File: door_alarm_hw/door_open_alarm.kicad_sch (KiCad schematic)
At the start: 62 parts, among them Q1 CJ2301 S1, Q2 BSS138PW,115, Q3 CJ2301 S1, SW1 TS-1088-AR02016, SW2 TS-1088-AR02016, SW3 SS-12D10L5, SW4 MET-200, U1 ESP32-S3-MINI-1, U2 AP2114HA-3.3TRG1

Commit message: Overhauling...
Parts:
- removed C1, C6, C7, C8: 1u, pepy_sym_lib:[CAP_SMD]0805_2012Metric, symbol pepy_sym_lib:[CAP_SMD]0805_2012Metric
- removed C2: 10u, pepy_sym_lib:[CAP_SMD]0805_2012Metric, symbol pepy_sym_lib:[CAP_SMD]0805_2012Metric
- removed C3: 0.1u, pepy_sym_lib:[CAP_SMD]0805_2012Metric, symbol pepy_sym_lib:[CAP_SMD]0805_2012Metric
- removed C4, C5: 22u, pepy_sym_lib:[CAP_SMD]0805_2012Metric, symbol pepy_sym_lib:[CAP_SMD]0805_2012Metric
- removed H2, H3, H4: MountingHole_Pad, symbol Mechanical:MountingHole_Pad
- removed R1, R3: 470R, pepy_sym_lib:[RES_SMD]0805_2012Metric, symbol pepy_sym_lib:[RES_SMD]0805_2012Metric
- removed R10: 1k, pepy_sym_lib:[RES_SMD]0805_2012Metric, symbol pepy_sym_lib:[RES_SMD]0805_2012Metric
- removed R11, R9: 15k 1%, pepy_sym_lib:[RES_SMD]0805_2012Metric, symbol pepy_sym_lib:[RES_SMD]0805_2012Metric
- removed R12, R13, R14, R16, R17, R6, R7: 10k, pepy_sym_lib:[RES_SMD]0805_2012Metric, symbol pepy_sym_lib:[RES_SMD]0805_2012Metric
- removed R15: 30k, pepy_sym_lib:[RES_SMD]0805_2012Metric, symbol pepy_sym_lib:[RES_SMD]0805_2012Metric
- removed R2, R4: 5.1k, pepy_sym_lib:[RES_SMD]0805_2012Metric, symbol pepy_sym_lib:[RES_SMD]0805_2012Metric
- removed R5: 1M, pepy_sym_lib:[RES_SMD]0805_2012Metric, symbol pepy_sym_lib:[RES_SMD]0805_2012Metric
- removed R8: 100k, pepy_sym_lib:[RES_SMD]0805_2012Metric, symbol pepy_sym_lib:[RES_SMD]0805_2012Metric
- removed REED_G1: GND, symbol Connector:TestPoint
- removed REED_OUT1: REED_OUT, symbol Connector:TestPoint
- removed TP11: REED, pepy_sym_lib:[TEST_POINT]TestPoint_Pad_D1.0mm, symbol Connector:TestPoint
- removed TP2: 3.3V, pepy_sym_lib:[TEST_POINT]TestPoint_Pad_D1.0mm, symbol Connector:TestPoint
- removed TP6: V_INPUT, pepy_sym_lib:[TEST_POINT]TestPoint_Pad_D1.0mm, symbol Connector:TestPoint
- added C1, C3, C7: CL21A106KOQNNNE, pepy_sym_lib:[CAP_SMD_0805_2012Metric], symbol pepy_sym_lib:[CAP_SMD_0805_2012Metric]Samsung Electro-Mechanics CL21A106KOQNNNE
- added C2, C8: CC0805KRX7R9BB104, pepy_sym_lib:[CAP_SMD_0805_2012Metric], symbol pepy_sym_lib:[CAP_SMD_0805_2012Metric]YAGEO CC0805KRX7R9BB104
- added C4, C5, C6: C0805C105M4VACTU, pepy_sym_lib:[CAP_SMD_0805_2012Metric], symbol pepy_sym_lib:[CAP_SMD_0805_2012Metric]KEMET C0805C105M4VACTU
- added F1: 0466.200NRHF, pepy_sym_lib:[FUSE_SMD_1206], symbol pepy_sym_lib:[FUSE_SMD_1206]Littelfuse 0466.200NRHF
- added MH1, MH2: ~, pepy_sym_lib:[MOUNTING_HOLE]MountingHole_2.2mm_M2_DIN965_Pad, symbol pepy_sym_lib:[MOUNTING_HOLE]MountingHole_Pad
- added R1, R10, R12, R15, R2, R5, R7, R9: 0805W8F1002T5E, pepy_sym_lib:[RES_SMD_0805_2012Metric], symbol pepy_sym_lib:[RES_SMD_0805_2012Metric]UNI-ROYAL(Uniroyal Elec) 0805W8F1002T5E
- added R11: 0805W8F1003T5E, pepy_sym_lib:[RES_SMD_0805_2012Metric], symbol pepy_sym_lib:[RES_SMD_0805_2012Metric]UNI-ROYAL(Uniroyal Elec) 0805W8F1003T5E
- added R13, R3, R4: 0805W8F5101T5E, pepy_sym_lib:[RES_SMD_0805_2012Metric], symbol pepy_sym_lib:[RES_SMD_0805_2012Metric]UNI-ROYAL(Uniroyal Elec) 0805W8F5101T5E
- added R14: 0805W8J0203T5E, pepy_sym_lib:[RES_SMD_0805_2012Metric], symbol pepy_sym_lib:[RES_SMD_0805_2012Metric]UNI-ROYAL(Uniroyal Elec) 0805W8J0203T5E
- added R16, R17: 0805W8F4700T5E, pepy_sym_lib:[RES_SMD_0805_2012Metric], symbol pepy_sym_lib:[RES_SMD_0805_2012Metric]UNI-ROYAL(Uniroyal Elec) 0805W8F4700T5E
- added R6: 0805W8F1004T5E, pepy_sym_lib:[RES_SMD_0805_2012Metric], symbol pepy_sym_lib:[RES_SMD_0805_2012Metric]UNI-ROYAL(Uniroyal Elec) 0805W8F1004T5E
- added R8: 0805W8F1001T5E, pepy_sym_lib:[RES_SMD_0805_2012Metric], symbol pepy_sym_lib:[RES_SMD_0805_2012Metric]UNI-ROYAL(Uniroyal Elec) 0805W8F1001T5E
- added TP5: 3.3V, pepy_sym_lib:[TEST_POINT]TestPoint_Pad_D1.0mm, symbol pepy_sym_lib:[TEST_POINT]TestPoint
- added TP6: GND, pepy_sym_lib:[TEST_POINT]TestPoint_Pad_D1.0mm, symbol pepy_sym_lib:[TEST_POINT]TestPoint
- added TP9: REED, pepy_sym_lib:[TEST_POINT]TestPoint_Pad_D1.0mm, symbol pepy_sym_lib:[TEST_POINT]TestPoint
- D1: renamed from D6; Manufacturer (none) -> STMicroelectronics; Package (none) -> SOD-123
- D2: renamed from D4; Manufacturer (none) -> STMicroelectronics; Package (none) -> SOD-123
- D3: renamed from D1; Manufacturer (none) -> Nexperia; Package (none) -> SOT1176-1
- D4: renamed from D5; Manufacturer (none) -> STMicroelectronics; Package (none) -> SOD-123
- D5: renamed from D2; Manufacturer (none) -> Lite-On; Package (none) -> 0603
- D6: renamed from D3; Manufacturer (none) -> Lite-On; Package (none) -> 0603
- FID1, FID2, FID3: value ~ -> Fiducial; footprint (none) -> Fiducial:Fiducial_0.5mm_Mask1mm
- H1: Manufacturer (none) -> XFCN
- J1: renamed from USB1; Manufacturer (none) -> SHOU HAN
- L1: Manufacturer (none) -> Murata Electronics
- Q1: renamed from Q2; Manufacturer (none) -> Nexperia; Package (none) -> SOT-323-3
- Q2: renamed from Q1; Manufacturer (none) -> Jiangsu Changjing Electronics Technology Co., Ltd.; Package (none) -> SOT-23
- Q3: Manufacturer (none) -> Jiangsu Changjing Electronics Technology Co., Ltd.; Package (none) -> SOT-23
- S1: renamed from SW3; Manufacturer (none) -> XKB Connection; Package (none) -> THT
- S2: renamed from SW1; Manufacturer (none) -> XUNPU
- S3: renamed from SW2; Manufacturer (none) -> XUNPU
- SW1: renamed from SW4; value MET-200 -> SW_Reed
- TP11: renamed from TP4; value BOOT0 -> BOOT
- TP2: renamed from TP9; value VCC -> VBAT
- U1: renamed from U2; Manufacturer (none) -> Diodes Incorporated; Package (none) -> SOT-223-3
- U2: renamed from U1; LCSC Part (none) -> C2913206; Manufacturer (none) -> Espressif Systems; Package (none) -> SMD-41P
- renumbered TP8 to TP10, TP10 to TP3, TP5 to TP4, TP3 to TP7, TP7 to TP8
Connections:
- net +3.3V: now also C3.1, C7.1, C8.2, R1.2, R10.2, R12.2, R15.2, TP5.1
- net BOOT0: now also C5.2, R15.1
- net EN: now also R11.1
- net ESP_RESET: now also C4.2, R10.1
- net GND: now also D5.2 (C), D6.2 (C), C1.2, C2.2, C3.2, C4.1, C5.1, C6.1, C7.2, C8.1, MH1.1, MH2.1, R14.1, R2.1, R3.1, R4.1, R5.1, R6.2, R7.1, R9.1, TP6.1; no longer D5.1 (K), D6.1 (K)
- net LED_EN: now also R17.2
- net MEAS_EN: now also R8.1
- net REED: now also TP9.1
- net SHIELD: now also C2.1, R6.1
- net STRAP_3: now also R1.1, R2.2
- net STRAP_45: now also R5.2
- net STRAP_46: now also R7.2
- net VBUS: now also R16.2
- net VCC: now also F1.1; no longer S1.2
- net V_INPUT: now also C1.1, R11.2
- net V_SENSE: now also C6.2, R13.1, R14.2
- net at Q3.2 (S): now also R12.1
- net at Q2.3 (D): now also R13.2
- net at Q1.1 (G): now also R8.2, R9.2
- net at J1.10 (CC2): now also R4.2
- net at J1.4 (CC1): now also R3.2
- new net: F1.2, S1.2
- new net: D6.1 (A), R17.1
- new net: D5.1 (A), R16.1
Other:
- moved on the sheet: D1, D2, D3, D4, D5, D6, FID1, FID2, FID3, H1, J1, Q1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

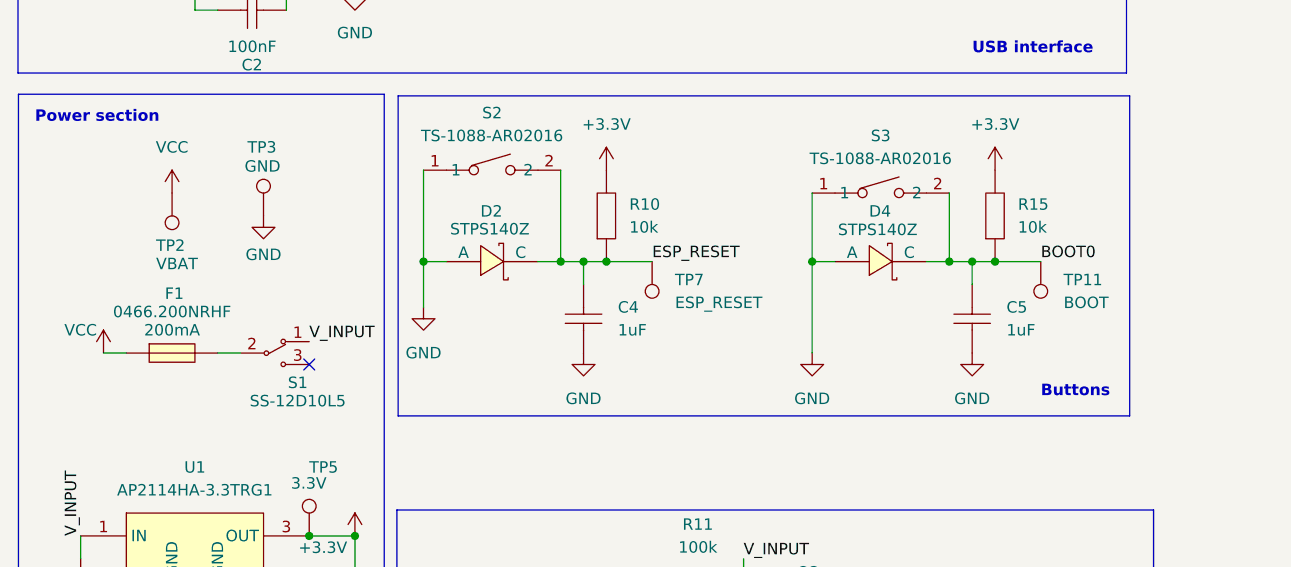
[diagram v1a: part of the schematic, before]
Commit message: Changes due to library update (minor)
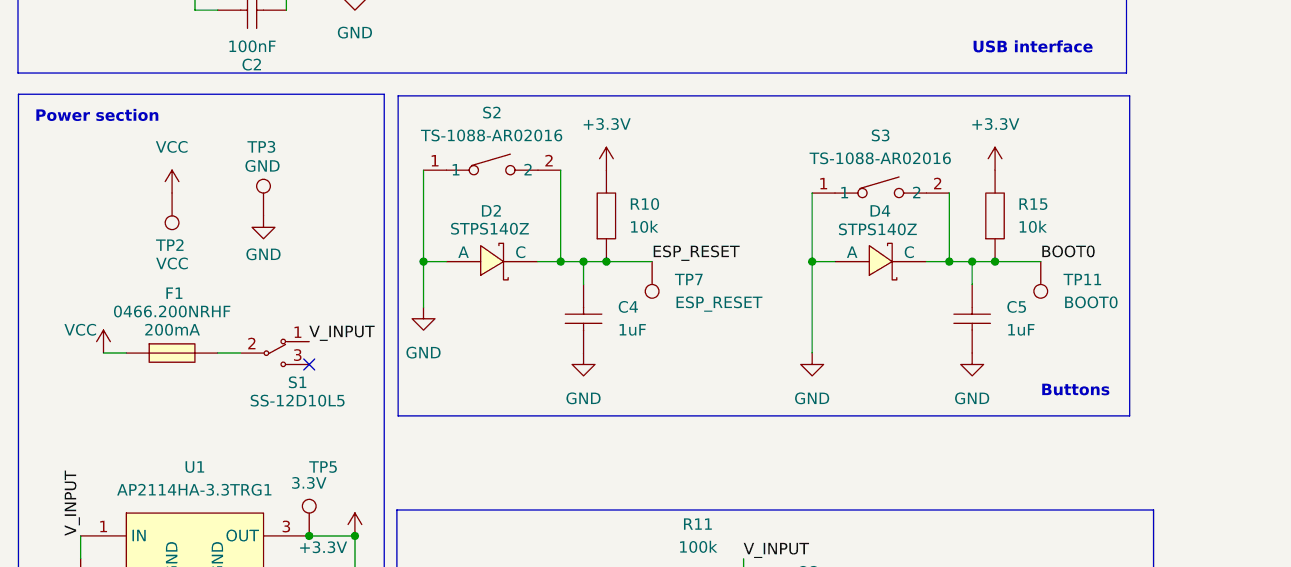
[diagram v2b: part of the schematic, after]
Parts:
- TP11: value BOOT -> BOOT0
- TP2: value VBAT -> VCC
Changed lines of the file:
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@@
 			)
 		)
-		(property "Description" " 20V 2.3A 350mW 112mΩ@4.5V,2.8A 1V@250uA 1PCSPChannel SOT-23 MOSFETs ROHS"
+		(property "Description" "20V 2.3A 350mW 112mΩ@4.5V,2.8A 1V@250uA 1PCSPChannel SOT-23 MOSFETs ROHS"
 			(at 99.06 223.52 0)
 			(effects
@@
 			)
 		)
-		(property "Description" "16V 10uF X5R ±10% 0805 Multilayer Ceramic Capacitors MLCC - SMD/SMT ROHS "
+		(property "Description" "16V 10uF X5R ±10% 0805 Multilayer Ceramic Capacitors MLCC - SMD/SMT ROHS"
 			(at 293.624 107.95 0)
 			(effects
@@
 			)
 		)
-		(property "Description" "16V 10uF X5R ±10% 0805 Multilayer Ceramic Capacitors MLCC - SMD/SMT ROHS "
+		(property "Description" "16V 10uF X5R ±10% 0805 Multilayer Ceramic Capacitors MLCC - SMD/SMT ROHS"
 			(at 39.624 163.83 0)
 			(effects
@@
 		)
 		(property "Description" "Smallsized module supporting 2.4 GHz WiFi (802.11 b/g/n) and Bluetooth ® 5 (LE) Built around ESP32S3 series of SoCs, Xtensa ® dualcore 32bit LX7 microprocessor Flash up to 8 MB, optional 2 MB PSRAM in chip package 39 GPIOs, rich set of peripherals Onboard PCB antenna or external antenna connector"
-			(at 236.22 66.04 0)
+			(at 236.982 119.38 0)
 			(effects
 				(font
@@
 		)
 		(property "LCSC Part" "C2913206"
-			(at 236.22 66.04 0)
+			(at 235.458 128.016 0)
 			(effects
 				(font
@@
 			)
 		)
-		(property "Description" " 20V 2.3A 350mW 112mΩ@4.5V,2.8A 1V@250uA 1PCSPChannel SOT-23 MOSFETs ROHS"
+		(property "Description" "20V 2.3A 350mW 112mΩ@4.5V,2.8A 1V@250uA 1PCSPChannel SOT-23 MOSFETs ROHS"
 			(at 99.06 165.1 0)
 			(effects
@@
 			)
 		)
-		(property "Value" "BOOT"
+		(property "Value" "BOOT0"
 			(at 132.08 129.032 0)
 			(effects
@@
 			)
 		)
-		(property "Description" " 125mW Thick Film Resistors 150V ±100ppm/℃ ±5% 20kΩ 0805 Chip Resistor - Surface Mount ROHS"
+		(property "Description" "125mW Thick Film Resistors 150V ±100ppm/℃ ±5% 20kΩ 0805 Chip Resistor - Surface Mount ROHS"
 			(at 124.206 177.8 0)
 			(effects
@@
 			)
 		)
-		(property "Description" " 20mA 99mcd Colorless transparent lens -30℃~+85℃ 631nm Red 130° 62.5mW 2V 0603 LED Indication - Discrete ROHS"
+		(property "Description" "20mA 99mcd Colorless transparent lens -30℃~+85℃ 631nm Red 130° 62.5mW 2V 0603 LED Indication - Discrete ROHS"
 			(at 147.32 66.04 0)
 			(effects
@@
 			)
 		)
-		(property "Description" "50V 100nF X7R ±10% 0805 Multilayer Ceramic Capacitors MLCC - SMD/SMT ROHS "
+		(property "Description" "50V 100nF X7R ±10% 0805 Multilayer Ceramic Capacitors MLCC - SMD/SMT ROHS"
 			(at 328.676 107.95 0)
 			(effects
@@
 			)
 		)
-		(property "Description" " 5A 1 Horizontal attachment 16P Female -25℃~+85℃ Type-C SMD USB Connectors ROHS"
+		(property "Description" "5A 1 Horizontal attachment 16P Female -25℃~+85℃ Type-C SMD USB Connectors ROHS"
 			(at 62.23 41.91 0)
 			(effects
@@
 			)
 		)
-		(property "Description" " 60V 320mA 1.6Ω@10V,300mA 1.5V@250uA 1PCSNChannel SOT-323-3 MOSFETs ROHS"
+		(property "Description" "60V 320mA 1.6Ω@10V,300mA 1.5V@250uA 1PCSNChannel SOT-323-3 MOSFETs ROHS"
 			(at 86.36 175.26 0)
 			(effects
@@
 			)
 		)
-		(property "Description" " 20mA 99mcd Colorless transparent lens -30℃~+85℃ 631nm Red 130° 62.5mW 2V 0603 LED Indication - Discrete ROHS"
+		(property "Description" "20mA 99mcd Colorless transparent lens -30℃~+85℃ 631nm Red 130° 62.5mW 2V 0603 LED Indication - Discrete ROHS"
 			(at 147.32 35.56 0)
 			(effects
@@
 			)
 		)
-		(property "Value" "VBAT"
+		(property "Value" "VCC"
 			(at 31.242 124.714 0)
 			(effects
@@
 			)
 		)
+		(property "Field5" ""
+			(at 33.02 116.84 0)
+			(effects
+				(font
+					(size 1.27 1.27)
+				)
+				(hide yes)
+			)
+		)
 		(pin "1"
 		)
@@
 			)
 		)
-		(property "Description" "50V 100nF X7R ±10% 0805 Multilayer Ceramic Capacitors MLCC - SMD/SMT ROHS "
+		(property "Description" "50V 100nF X7R ±10% 0805 Multilayer Ceramic Capacitors MLCC - SMD/SMT ROHS"
 			(at 41.91 110.236 0)
 			(effects
@@
 			)
 		)
-		(property "Description" "16V 10uF X5R ±10% 0805 Multilayer Ceramic Capacitors MLCC - SMD/SMT ROHS "
+		(property "Description" "16V 10uF X5R ±10% 0805 Multilayer Ceramic Capacitors MLCC - SMD/SMT ROHS"
 			(at 9.144 161.29 0)
 			(effects
